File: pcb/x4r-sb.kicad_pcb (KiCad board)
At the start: 2 copper layers, 36 x 36 mm, 25 parts, among them P1 CONN_01X04, P2 CONN_02X06, P3 CONN_01X02, Q1 Q_NMOS_GSD, U1 SN74AUP3G06

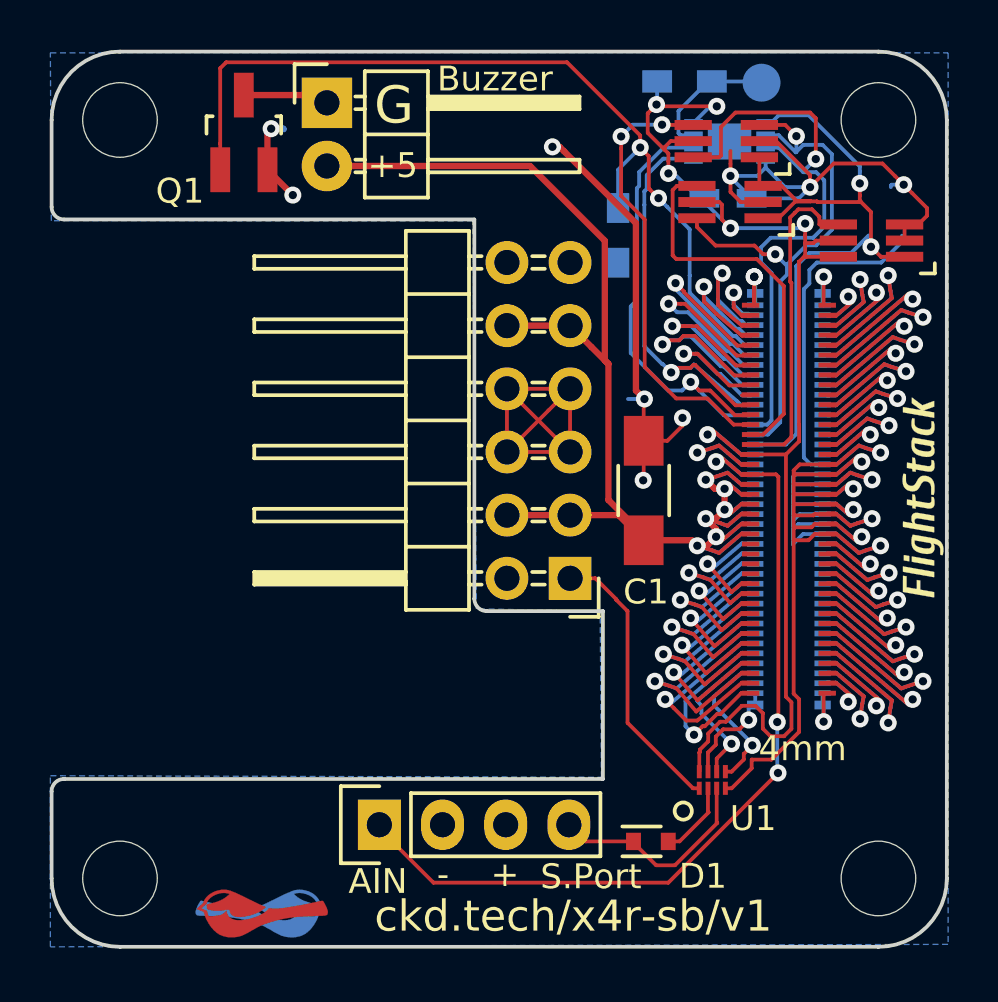
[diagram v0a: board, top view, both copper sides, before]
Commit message: v2 of x4r cradle that switchs to an XOR inverter gate. Also shifts the buzzer pins a little.
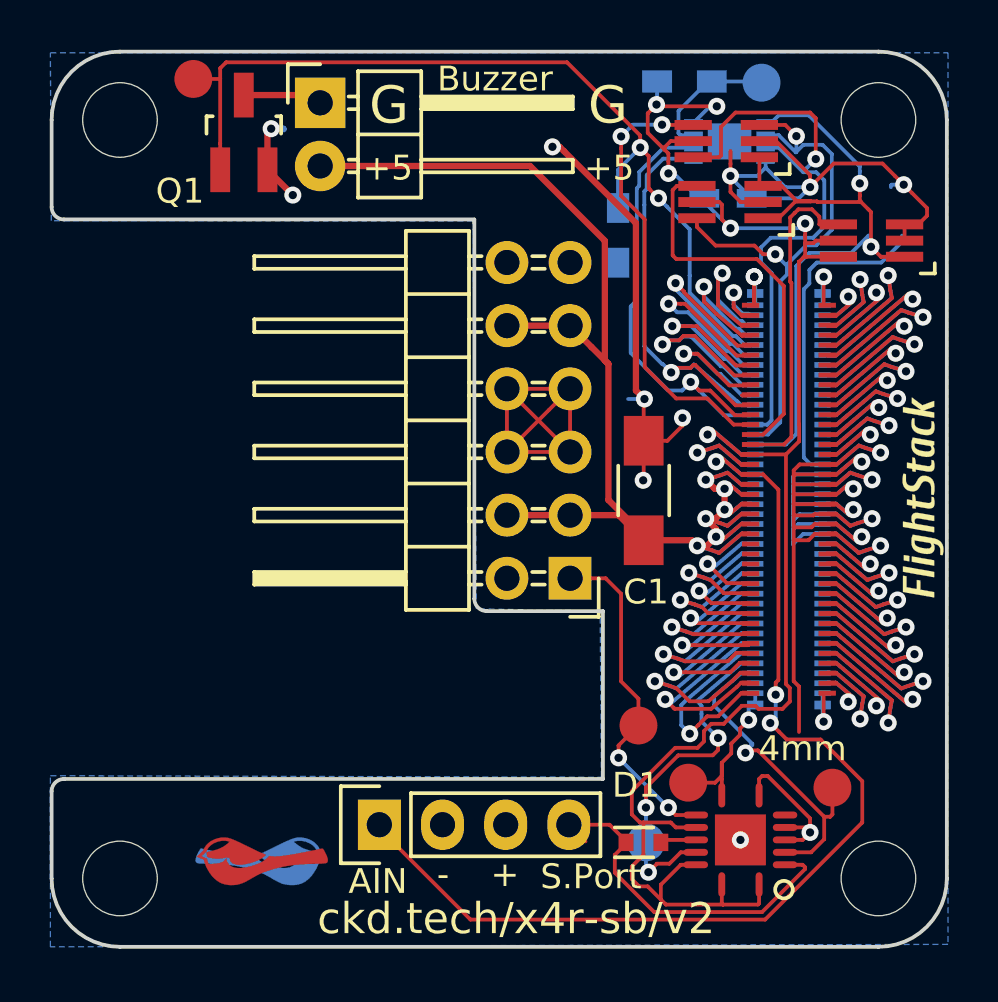
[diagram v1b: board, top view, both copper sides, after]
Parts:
- added P10: CONN_01X01, Measurement_Points:Measurement_Point_Round-SMD-Pad_Small, F.Cu at (135.7, 91.1)
- added P5: CONN_01X01, Measurement_Points:Measurement_Point_Round-SMD-Pad_Small, F.Cu at (153.6, 117.1)
- added P7: CONN_01X01, Measurement_Points:Measurement_Point_Round-SMD-Pad_Small, F.Cu at (155.6, 119.4)
- added P8: CONN_01X01, Measurement_Points:Measurement_Point_Round-SMD-Pad_Small, F.Cu at (161.4, 119.6)
- added P9: CONN_01X01, Measurement_Points:Measurement_Point_Round-SMD-Pad_Small, B.Cu at (153.9, 121.8)
- PORT_IN1: footprint DF40-80pin-Header -> hirose-df40:DF40-80pin-Header
- PORT_OUT1: footprint DF40-3-4mm-80pin-Receptacle -> hirose-df40:DF40-3-4mm-80pin-Receptacle
- U1: value SN74AUP3G06 -> 74LS86; footprint 8-XFDFN -> QFN-14-3.5x3.5mm
- moved U1 2.66 mm to (157.7, 121.7), turned to 180 degrees
- moved G*** 2.10 mm to (138.4, 122.6) (x2)
- moved D1 0.30 mm to (153.8, 121.8)
- moved P3 0.27 mm to (140.8, 92.1)
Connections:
- C1 pad 2: GNDPWR -> GND
- P1 pad 2: GNDPWR -> GND
- P2 pad 5: GNDPWR -> GND
- P2 pad 6: GNDPWR -> GND
- P2 pad 7: GNDPWR -> GND
- P2 pad 8: GNDPWR -> GND
- PORT_ANDOR1 pad 2: GNDPWR -> GND
- PORT_C1 pad 2: GNDPWR -> GND
- PORT_IC1 pad 4: GNDPWR -> GND
- PORT_IN1 pad 57: GNDPWR -> GND
- PORT_IN1 pad 58: GNDPWR -> GND
- PORT_IN1 pad 59: GNDPWR -> GND
- PORT_IN1 pad 60: GNDPWR -> GND
- PORT_IN1 pad 61: GNDPWR -> GND
- PORT_IN1 pad 62: GNDPWR -> GND
- PORT_IN1 pad 63: GNDPWR -> GND
- PORT_IN1 pad 64: GNDPWR -> GND
- PORT_INV1 pad 2: GNDPWR -> GND
- PORT_INV1 pad 3: GNDPWR -> GND
- PORT_OUT1 pad 57: GNDPWR -> GND
- PORT_OUT1 pad 58: GNDPWR -> GND
- PORT_OUT1 pad 59: GNDPWR -> GND
- PORT_OUT1 pad 60: GNDPWR -> GND
- PORT_OUT1 pad 61: GNDPWR -> GND
- PORT_OUT1 pad 62: GNDPWR -> GND
- PORT_OUT1 pad 63: GNDPWR -> GND
- PORT_OUT1 pad 64: GNDPWR -> GND
- PORT_XOR1 pad 2: GNDPWR -> GND
- Q1 pad 2: GNDPWR -> GND
- R1 pad 2: GNDPWR -> GND
- U1 pad 1: /nRC_RX -> +3V3
- U1 pad 2: Net-(D1-Pad2) -> /S.Port
- U1 pad 3: /S.Port -> /ExpansionPort/UART2_RX
- U1 pad 4: GNDPWR -> GND
- U1 pad 5: /ExpansionPort/UART2_RX -> GND
- U1 pad 6: /ExpansionPort/UART2_TX -> Net-(U1-Pad6)
- U1 pad 7: /ExpansionPort/UART1_RX -> GND
- U1 pad 8: +3V3 -> /ExpansionPort/UART1_RX
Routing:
- net GND: track 0.00 -> 144.2 mm, vias 0 -> 19
- net GNDPWR: track 142.1 -> 0.00 mm, vias 17 -> 0
- net +3V3: track 53.7 -> 70.0 mm
- net /ExpansionPort/BATT_DIV: track 35.5 -> 43.4 mm
- net /ExpansionPort/UART2_TX: track 6.37 -> 14.2 mm, vias 1 -> 3
- net /ExpansionPort/UART2_RX: track 6.08 -> 13.4 mm
- net /S.Port: track 8.78 -> 14.9 mm
- net /ExpansionPort/UART1_RX: track 4.36 -> 6.69 mm
- net /nRC_RX: track 11.3 -> 13.6 mm, vias 0 -> 2
- net Net-(D1-Pad2): track 3.08 -> 1.45 mm
- net /ExpansionPort/GPIO1: track 35.6 -> 36.6 mm
- net /ExpansionPort/UART5_TX: track 7.27 -> 6.34 mm
- net /ExpansionPort/UART4_TX: track 8.17 -> 7.25 mm
- net /ExpansionPort/UART6_TX: track 6.38 -> 5.61 mm
- net /ExpansionPort/UART6_RX: track 7.83 -> 7.06 mm
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- added copper zone on B.Cu, net GND
- removed copper zone on B.Cu, net GNDPWR
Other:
- board text added: "ckd.tech/x4r-sb/v2"
- board text removed: "ckd.tech/x4r-sb/v1"
